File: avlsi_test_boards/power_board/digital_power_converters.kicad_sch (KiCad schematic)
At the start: 21 parts, among them U1 TLV1117LV18DCYR, U11 TLV75709PDBV, U2 TLV1117LV25DCYR, U3 TLV1117LV33DCYR, U4 DS04-254-2-04BK-SMT, U5 74HC4051D_653

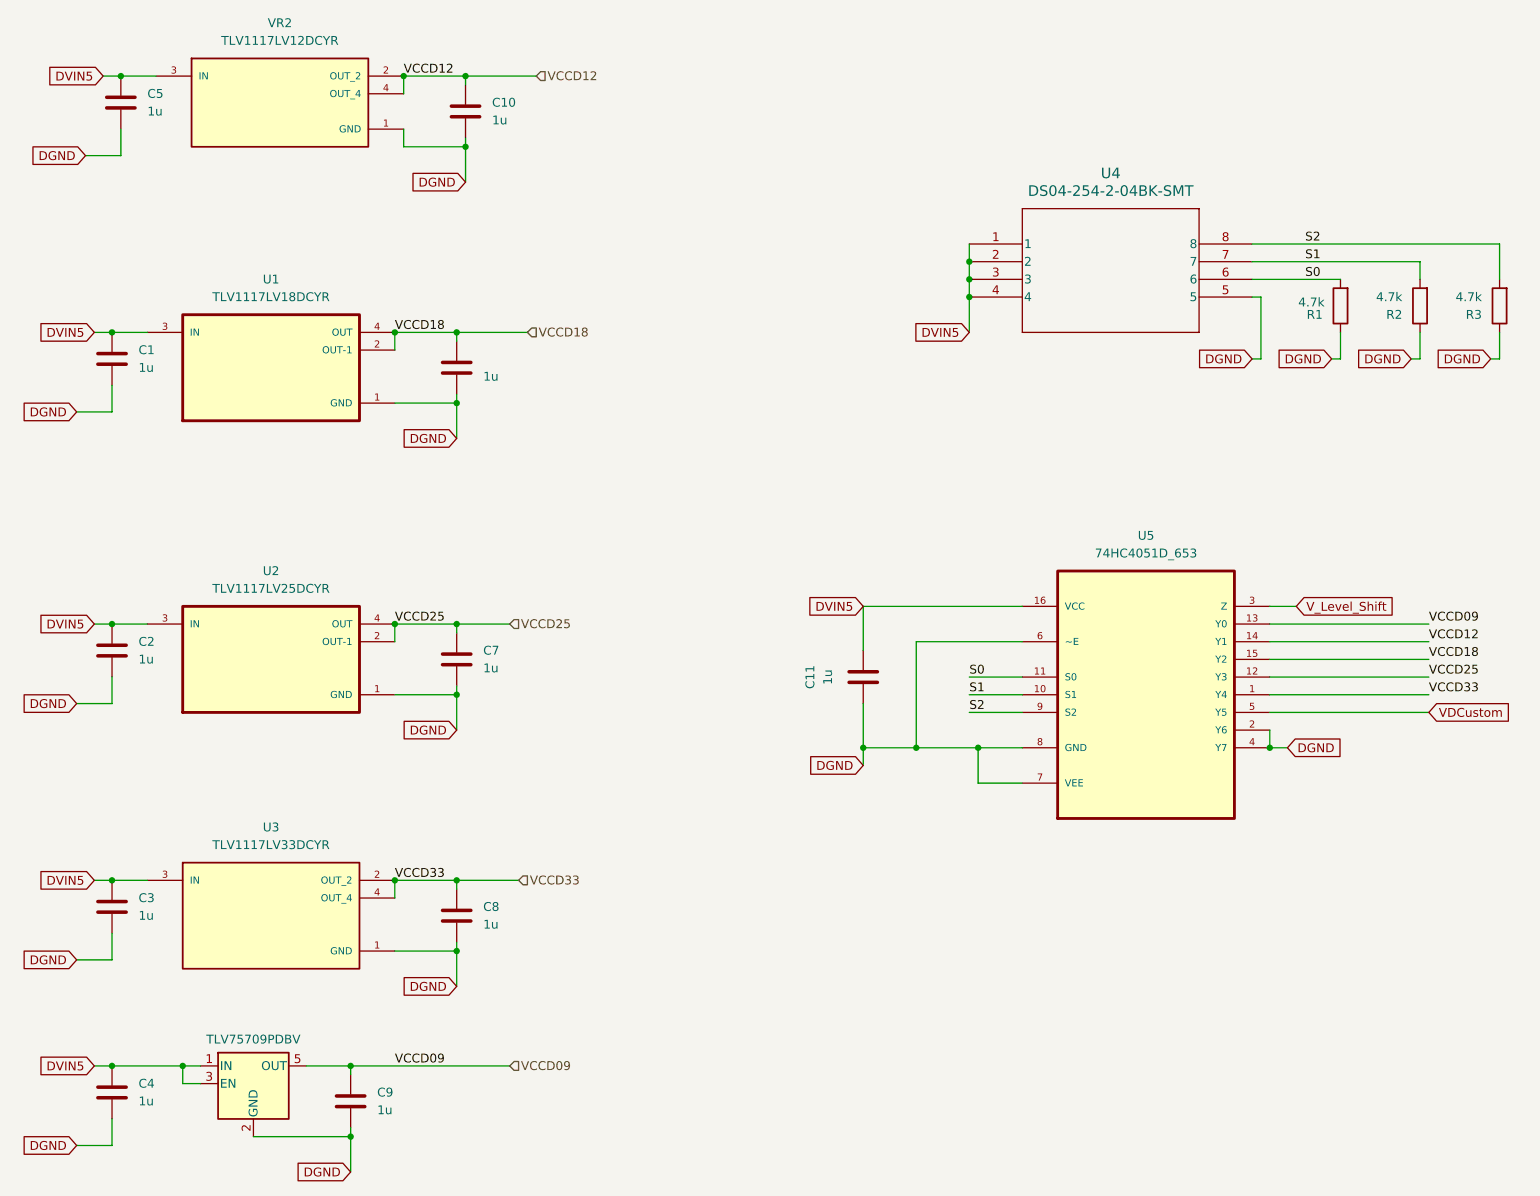
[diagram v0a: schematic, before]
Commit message: Add updated power board layout and schematic
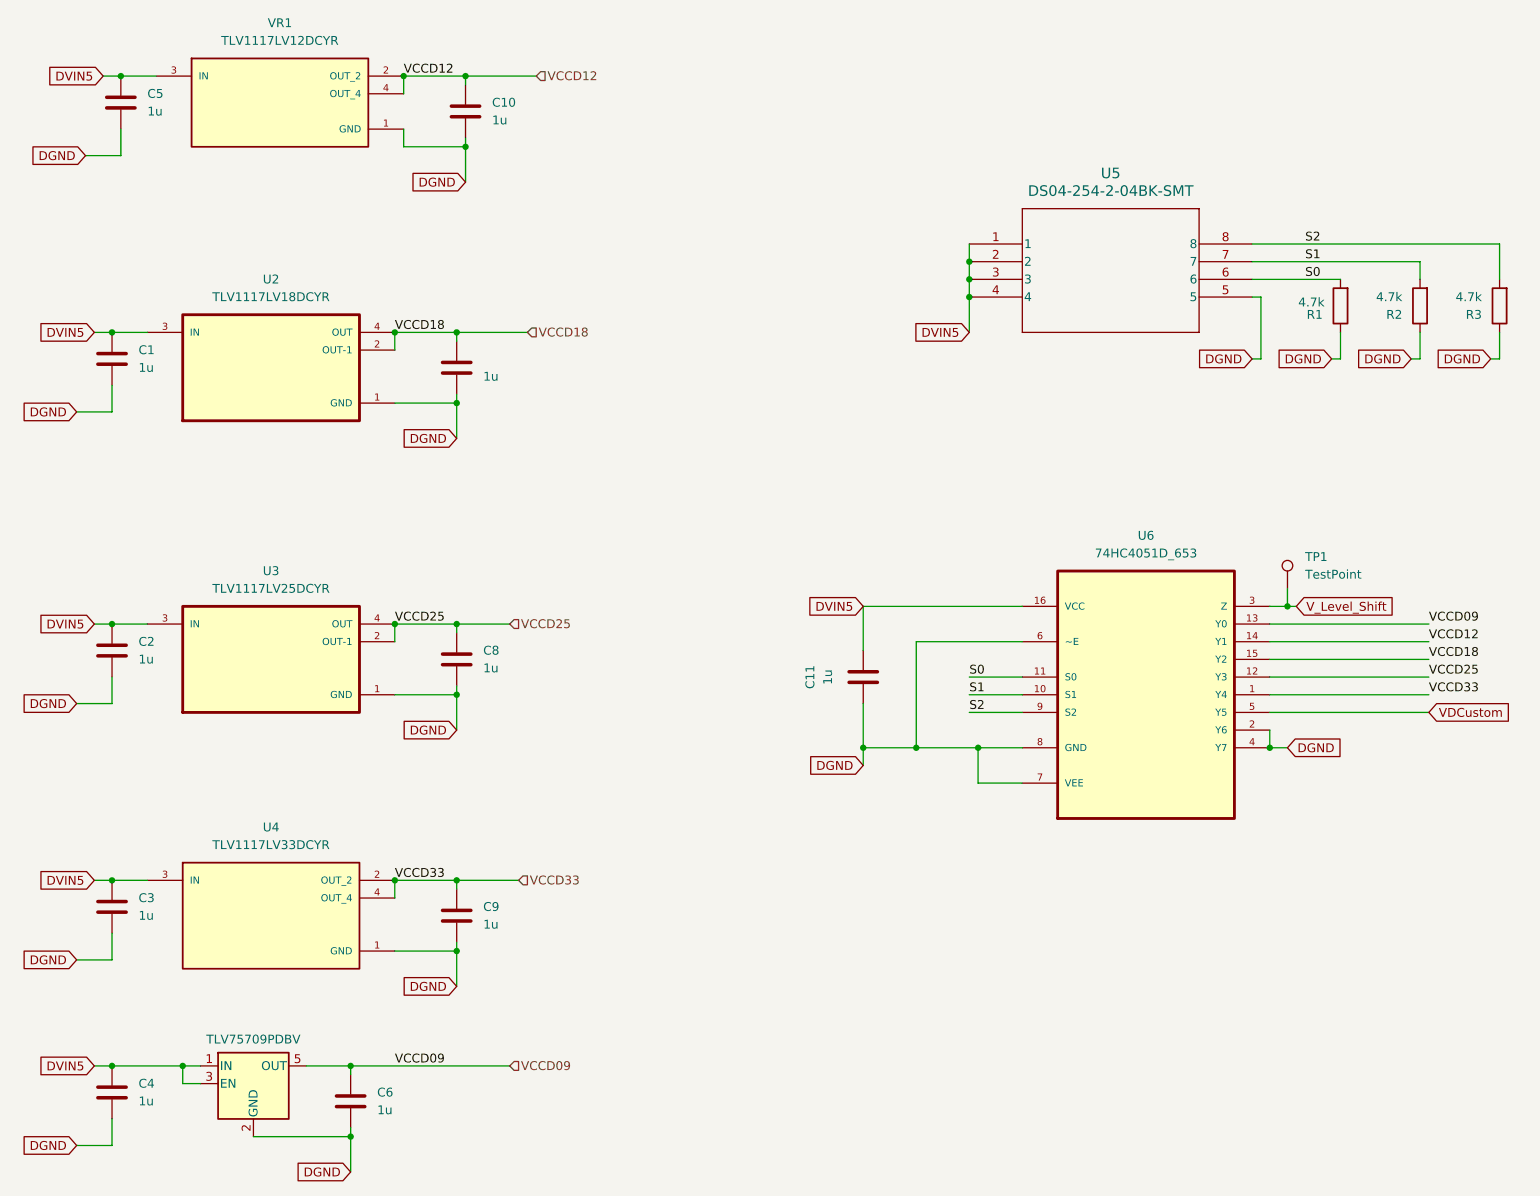
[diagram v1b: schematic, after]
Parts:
- added TP1: TestPoint, TestPoint:TestPoint_Loop_D3.80mm_Drill2.0mm, symbol Connector:TestPoint
- renumbered C9 to C6, C6 to C7, C7 to C8, C8 to C9, U11 to U1, U1 to U2, U2 to U3, U3 to U4, U4 to U5, U5 to U6, VR2 to VR1
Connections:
- net V_Level_Shift: now also TP1.1
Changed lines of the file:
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@@
 	)
 	(junction
+		(at 228.6 114.3)
+		(diameter 0)
+		(color 0 0 0 0)
+	)
+	(junction
 		(at 226.06 134.62)
 		(diameter 0)
@@
 	(wire
 		(pts
+			(xy 228.6 111.76) (xy 228.6 114.3)
+		)
+		(stroke
+			(width 0)
+			(type default)
+		)
+	)
+	(wire
+		(pts
 			(xy 167.64 134.62) (xy 167.64 128.27)
 		)
@@
 	(wire
 		(pts
-			(xy 226.06 114.3) (xy 229.87 114.3)
+			(xy 226.06 114.3) (xy 228.6 114.3)
 		)
 		(stroke
@@
 		)
 	)
+	(wire
+		(pts
+			(xy 228.6 114.3) (xy 229.87 114.3)
+		)
+		(stroke
+			(width 0)
+			(type default)
+		)
+	)
 	(label "VCCD25"
 		(at 248.92 124.46 0)
@@
 		(dnp no)
 		(fields_autoplaced yes)
-		(property "Reference" "VR2"
+		(property "Reference" "VR1"
 			(at 83.82 30.48 0)
 			(effects
@@
 			(project "power_board"
 				(path "/425e3f4e-d960-41c8-a4b7-4f888de39c97/572e1625-24a1-4783-bac1-8c305a89efd3"
-					(reference "VR2")
+					(reference "VR1")
 					(unit 1)
 				)
@@
 		(dnp no)
 		(fields_autoplaced yes)
-		(property "Reference" "C7"
+		(property "Reference" "C8"
 			(at 113.03 120.6499 0)
 			(effects
@@
 			(project "power_board"
 				(path "/425e3f4e-d960-41c8-a4b7-4f888de39c97/572e1625-24a1-4783-bac1-8c305a89efd3"
-					(reference "C7")
+					(reference "C8")
 					(unit 1)
 				)
@@
 		(dnp no)
 		(fields_autoplaced yes)
-		(property "Reference" "U2"
+		(property "Reference" "U3"
 			(at 82.55 109.22 0)
 			(effects
@@
 			(project "power_board"
 				(path "/425e3f4e-d960-41c8-a4b7-4f888de39c97/572e1625-24a1-4783-bac1-8c305a89efd3"
-					(reference "U2")
+					(reference "U3")
 					(unit 1)
 				)
@@
 		(dnp no)
 		(fields_autoplaced yes)
-		(property "Reference" "C8"
+		(property "Reference" "C9"
 			(at 113.03 157.4799 0)
 			(effects
@@
 			(project "power_board"
 				(path "/425e3f4e-d960-41c8-a4b7-4f888de39c97/572e1625-24a1-4783-bac1-8c305a89efd3"
-					(reference "C8")
+					(reference "C9")
 					(unit 1)
 				)
@@
 		(dnp no)
 		(fields_autoplaced yes)
-		(property "Reference" "U11"
+		(property "Reference" "U1"
 			(at 80.01 173.99 0)
 			(effects
@@
 			(project "power_board"
 				(path "/425e3f4e-d960-41c8-a4b7-4f888de39c97/572e1625-24a1-4783-bac1-8c305a89efd3"
-					(reference "U11")
+					(reference "U1")
 					(unit 1)
 				)
@@
 		(dnp no)
 		(fields_autoplaced yes)
-		(property "Reference" "C9"
+		(property "Reference" "C6"
 			(at 97.79 184.1499 0)
 			(effects
@@
 			(project "power_board"
 				(path "/425e3f4e-d960-41c8-a4b7-4f888de39c97/572e1625-24a1-4783-bac1-8c305a89efd3"
-					(reference "C9")
+					(reference "C6")
 					(unit 1)
 				)
@@
 		(dnp no)
 		(fields_autoplaced yes)
-		(property "Reference" "U1"
+		(property "Reference" "U2"
 			(at 82.55 67.31 0)
 			(effects
@@
 			(project "power_board"
 				(path "/425e3f4e-d960-41c8-a4b7-4f888de39c97/572e1625-24a1-4783-bac1-8c305a89efd3"
-					(reference "U1")
+					(reference "U2")
 					(unit 1)
 				)
@@
 		(dnp no)
 		(fields_autoplaced yes)
-		(property "Reference" "C6"
+		(property "Reference" "C7"
 			(at 113.03 78.7399 0)
 			(effects
@@
 			(project "power_board"
 				(path "/425e3f4e-d960-41c8-a4b7-4f888de39c97/572e1625-24a1-4783-bac1-8c305a89efd3"
-					(reference "C6")
+					(reference "C7")
+					(unit 1)
+				)
+			)
+		)
+	)
+	(symbol
+		(lib_id "Connector:TestPoint")
+		(at 228.6 111.76 0)
+		(unit 1)
+		(exclude_from_sim no)
+		(in_bom yes)
+		(on_board yes)
+		(dnp no)
+		(fields_autoplaced yes)
+		(property "Reference" "TP1"
+			(at 231.14 107.1879 0)
+			(effects
+				(font
+					(size 1.27 1.27)
+				)
+				(justify left)
+			)
+		)
+		(property "Value" "TestPoint"
+			(at 231.14 109.7279 0)
+			(effects
+				(font
+					(size 1.27 1.27)
+				)
+				(justify left)
+			)
+		)
+		(property "Footprint" "TestPoint:TestPoint_Loop_D3.80mm_Drill2.0mm"
+			(at 233.68 111.76 0)
+			(effects
+				(font
+					(size 1.27 1.27)
+				)
+				(hide yes)
+			)
+		)
+		(property "Datasheet" "~"
+			(at 233.68 111.76 0)
+			(effects
+				(font
+					(size 1.27 1.27)
+				)
+				(hide yes)
+			)
+		)
+		(property "Description" "test point"
+			(at 228.6 111.76 0)
+			(effects
+				(font
+					(size 1.27 1.27)
+				)
+				(hide yes)
+			)
+		)
+		(pin "1"
+		)
+		(instances
+			(project ""
+				(path "/425e3f4e-d960-41c8-a4b7-4f888de39c97/572e1625-24a1-4783-bac1-8c305a89efd3"
+					(reference "TP1")
 					(unit 1)
 				)
@@
 		(dnp no)
 		(fields_autoplaced yes)
-		(property "Reference" "U5"
+		(property "Reference" "U6"
 			(at 208.28 104.14 0)
 			(effects
@@
 			(project "power_board"
 				(path "/425e3f4e-d960-41c8-a4b7-4f888de39c97/572e1625-24a1-4783-bac1-8c305a89efd3"
-					(reference "U5")
+					(reference "U6")
 					(unit 1)
 				)
@@
 		(dnp no)
 		(fields_autoplaced yes)
-		(property "Reference" "U4"
+		(property "Reference" "U5"
 			(at 203.2 52.07 0)
 			(effects
@@
 			(project "power_board"
 				(path "/425e3f4e-d960-41c8-a4b7-4f888de39c97/572e1625-24a1-4783-bac1-8c305a89efd3"
-					(reference "U4")
+					(reference "U5")
 					(unit 1)
 				)
@@
 		(on_board yes)
 		(dnp no)
-		(property "Reference" "U3"
+		(property "Reference" "U4"
 			(at 82.55 146.05 0)
 			(effects
@@
 			(project "power_board"
 				(path "/425e3f4e-d960-41c8-a4b7-4f888de39c97/572e1625-24a1-4783-bac1-8c305a89efd3"
-					(reference "U3")
+					(reference "U4")
 					(unit 1)
 				)

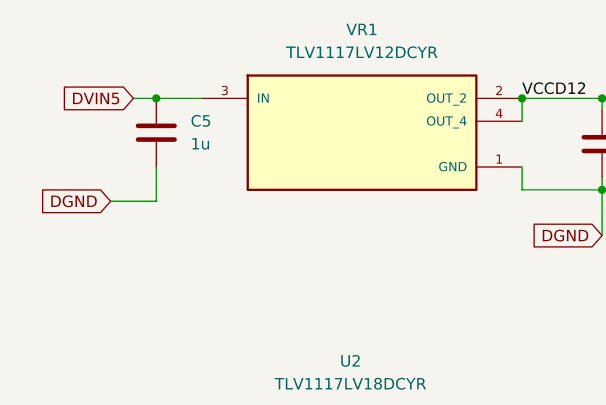
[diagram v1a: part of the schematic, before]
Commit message: Add power board
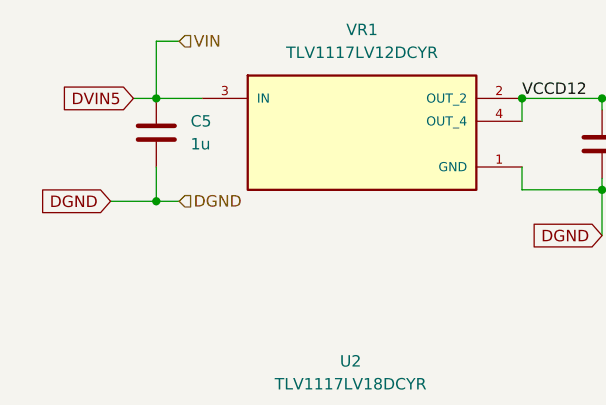
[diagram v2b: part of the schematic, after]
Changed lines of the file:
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@@
+	)
+	(junction
+		(at 60.96 49.53)
+		(diameter 0)
+		(color 0 0 0 0)
 	)
 	(junction
@@
 	(wire
 		(pts
+			(xy 60.96 49.53) (xy 63.5 49.53)
+		)
+		(stroke
+			(width 0)
+			(type default)
+		)
+	)
+	(wire
+		(pts
 			(xy 101.6 48.26) (xy 110.49 48.26)
 		)
@@
 	(wire
 		(pts
+			(xy 60.96 31.75) (xy 60.96 38.1)
+		)
+		(stroke
+			(width 0)
+			(type default)
+		)
+	)
+	(wire
+		(pts
 			(xy 100.33 116.84) (xy 100.33 119.38)
 		)
@@
 		(pts
 			(xy 109.22 74.93) (xy 109.22 76.2)
+		)
+		(stroke
+			(width 0)
+			(type default)
+		)
+	)
+	(wire
+		(pts
+			(xy 63.5 31.75) (xy 60.96 31.75)
 		)
 		(stroke
@@
 		(effects
 			(font
+				(size 1.27 1.27)
+			)
+			(justify left)
+		)
+	)
+	(hierarchical_label "DGND"
+		(shape input)
+		(at 63.5 49.53 0)
+		(effects
+			(font
+				(size 1.27 1.27)
+			)
+			(justify left)
+		)
+	)
+	(hierarchical_label "VIN"
+		(shape input)
+		(at 63.5 31.75 0)
+		(effects
+			(font
